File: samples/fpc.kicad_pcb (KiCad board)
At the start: 2 copper layers, 15.1 x 13.2 mm, 5 parts, among them J1 Conn_01x02_Pin

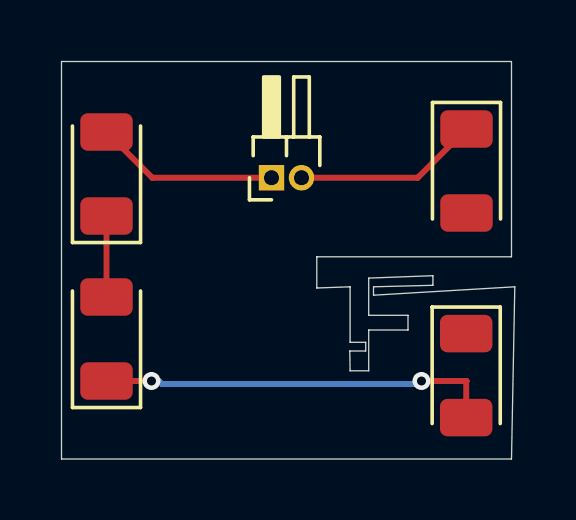
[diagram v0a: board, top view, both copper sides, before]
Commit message: update samples/{fpc,maze}
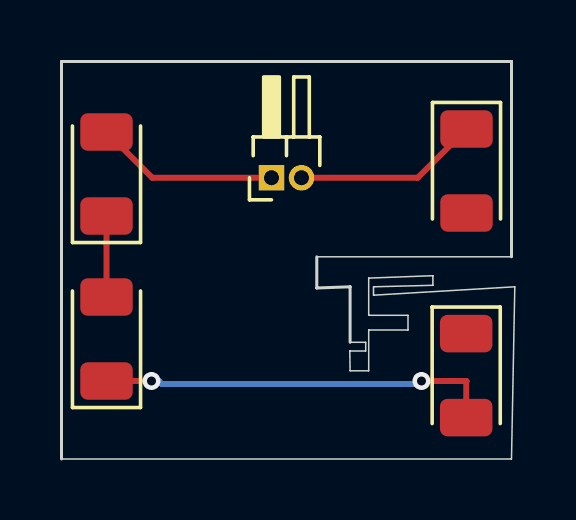
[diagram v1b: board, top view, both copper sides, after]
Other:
- board text added: "a=-40 r=0.5"
- board text added: "a=-45"
- board text added: "a=-60"
- board text added: "a=-65 r=0.5"
- board text added: "a=-70"
- board text added: "a=180"
- board text added: "a=30"
- board text added: "a=45"
- board text added: "a=50"
- board text added: "a=60"
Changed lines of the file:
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@@
 		(end 105.5 83.5)
 		(stroke
-			(width 0)
+			(width 0.1)
 			(type default)
 		)
@@
 		(end 90.5 83.5)
 		(stroke
-			(width 0)
+			(width 0.1)
 			(type default)
 		)
@@
 		(end 99.01 91.05)
 		(stroke
-			(width 0)
+			(width 0.1)
 			(type default)
 		)
@@
 		(end 100.12 91.01)
 		(stroke
-			(width 0)
+			(width 0.1)
 			(type default)
 		)
@@
 		(end 100.12 93.81)
 		(stroke
-			(width 0)
-			(type default)
+			(width 0.05)
+			(type solid)
 		)
 		(layer "Edge.Cuts")
@@
 		(end 100.12 92.86)
 		(stroke
-			(width 0)
+			(width 0.1)
 			(type default)
 		)
@@
 		(end 100.64 92.86)
 		(stroke
-			(width 0)
-			(type default)
+			(width 0.05)
+			(type solid)
 		)
 		(layer "Edge.Cuts")
@@
 		(end 100.74 93.81)
 		(stroke
-			(width 0)
-			(type default)
+			(width 0.05)
+			(type solid)
 		)
 		(layer "Edge.Cuts")
@@
 		(end 100.64 93.15)
 		(stroke
-			(width 0)
-			(type default)
+			(width 0.05)
+			(type solid)
 		)
 		(layer "Edge.Cuts")
@@
 		(end 100.11 93.15)
 		(stroke
-			(width 0)
-			(type default)
-		)
-		(layer "Edge.Cuts")
-	)
-	(gr_line
-		(start 100.74 90.72)
-		(end 102.88 90.64)
-		(stroke
-			(width 0)
-			(type default)
+			(width 0.05)
+			(type solid)
 		)
 		(layer "Edge.Cuts")
@@
 		(end 100.74 90.72)
 		(stroke
-			(width 0)
-			(type default)
+			(width 0.05)
+			(type solid)
 		)
 		(layer "Edge.Cuts")
@@
 		(end 102.05 92.45)
 		(stroke
-			(width 0)
-			(type default)
+			(width 0.05)
+			(type solid)
 		)
 		(layer "Edge.Cuts")
@@
 		(end 100.74 92.45)
 		(stroke
-			(width 0)
-			(type default)
+			(width 0.05)
+			(type solid)
 		)
 		(layer "Edge.Cuts")
@@
 	(gr_line
 		(start 100.9 91.01)
-		(end 100.9 91.29)
-		(stroke
-			(width 0)
+		(end 102.88 90.96)
+		(stroke
+			(width 0.05)
+			(type default)
+		)
+		(layer "Edge.Cuts")
+	)
+	(gr_line
+		(start 100.9 91.29)
+		(end 100.9 91.01)
+		(stroke
+			(width 0.05)
 			(type default)
 		)
@@
 		(end 105.61 91.01)
 		(stroke
-			(width 0)
-			(type default)
+			(width 0.05)
+			(type solid)
 		)
 		(layer "Edge.Cuts")
@@
 		(end 100.74 91.96)
 		(stroke
-			(width 0)
-			(type default)
+			(width 0.05)
+			(type solid)
 		)
 		(layer "Edge.Cuts")
@@
 		(end 102.05 91.96)
 		(stroke
-			(width 0)
-			(type default)
+			(width 0.05)
+			(type solid)
 		)
 		(layer "Edge.Cuts")
@@
 	(gr_line
 		(start 102.88 90.64)
-		(end 102.88 90.96)
-		(stroke
-			(width 0)
+		(end 100.74 90.72)
+		(stroke
+			(width 0.05)
 			(type default)
 		)
@@
 	(gr_line
 		(start 102.88 90.96)
-		(end 100.9 91.01)
-		(stroke
-			(width 0)
+		(end 102.88 90.64)
+		(stroke
+			(width 0.05)
 			(type default)
 		)
@@
 		(end 105.5 90.01)
 		(stroke
-			(width 0)
+			(width 0.1)
 			(type default)
 		)
@@
 		(end 99.01 90.01)
 		(stroke
-			(width 0)
-			(type default)
+			(width 0.05)
+			(type solid)
 		)
 		(layer "Edge.Cuts")
@@
 		(end 90.5 96.75)
 		(stroke
-			(width 0)
-			(type default)
+			(width 0.05)
+			(type solid)
 		)
 		(layer "Edge.Cuts")
@@
 		(end 105.5 96.75)
 		(stroke
-			(width 0)
-			(type default)
+			(width 0.05)
+			(type solid)
 		)
 		(layer "Edge.Cuts")
@@
 		(layer "User.4")
 	)
+	(gr_text "a=-70"
+		(at 94.655 97.345 270)
+		(layer "User.4")
+		(effects
+			(font
+				(size 0.2 0.2)
+				(thickness 0.01)
+			)
+			(justify left bottom)
+		)
+	)
+	(gr_text "a=180"
+		(at 95.505 97.395 270)
+		(layer "User.4")
+		(effects
+			(font
+				(size 0.2 0.2)
+				(thickness 0.01)
+			)
+			(justify left bottom)
+		)
+	)
+	(gr_text "a=-65 r=0.5"
+		(at 96.15 97.27 270)
+		(layer "User.4")
+		(effects
+			(font
+				(size 0.2 0.2)
+				(thickness 0.01)
+			)
+			(justify left bottom)
+		)
+	)
+	(gr_text "a=50"
+		(at 98.15 98.69 270)
+		(layer "User.4")
+		(effects
+			(font
+				(size 0.2 0.2)
+				(thickness 0.01)
+			)
+			(justify left bottom)
+		)
+	)
+	(gr_text "a=-45"
+		(at 100.22 92.52 270)
+		(layer "User.4")
+		(effects
+			(font
+				(size 0.2 0.2)
+				(thickness 0.01)
+			)
+			(justify left bottom)
+		)
+	)
+	(gr_text "a=-40 r=0.5"
+		(at 100.96 98.94 270)
+		(layer "User.4")
+		(effects
+			(font
+				(size 0.2 0.2)
+				(thickness 0.01)
+			)
+			(justify left bottom)
+		)
+	)
+	(gr_text "a=45"
+		(at 101.07 92.3 270)
+		(layer "User.4")
+		(effects
+			(font
+				(size 0.2 0.2)
+				(thickness 0.01)
+			)
+			(justify left bottom)
+		)
+	)
+	(gr_text "a=-60"
+		(at 101.305 97.235 270)
+		(layer "User.4")
+		(effects
+			(font
+				(size 0.2 0.2)
+				(thickness 0.01)
+			)
+			(justify left bottom)
+		)
+	)
+	(gr_text "a=-45"
+		(at 101.61 92.27 270)
+		(layer "User.4")
+		(effects
+			(font
+				(size 0.2 0.2)
+				(thickness 0.01)
+			)
+			(justify left bottom)
+		)
+	)
+	(gr_text "a=30"
+		(at 101.895 97.245 270)
+		(layer "User.4")
+		(effects
+			(font
+				(size 0.2 0.2)
+				(thickness 0.01)
+			)
+			(justify left bottom)
+		)
+	)
+	(gr_text "a=60"
+		(at 102.49 97.32 270)
+		(layer "User.4")
+		(effects
+			(font
+				(size 0.2 0.2)
+				(thickness 0.01)
+			)
+			(justify left bottom)
+		)
+	)
 	(segment
